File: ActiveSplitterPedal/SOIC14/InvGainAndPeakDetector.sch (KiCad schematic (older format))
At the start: 9 parts, among them U1 TL074

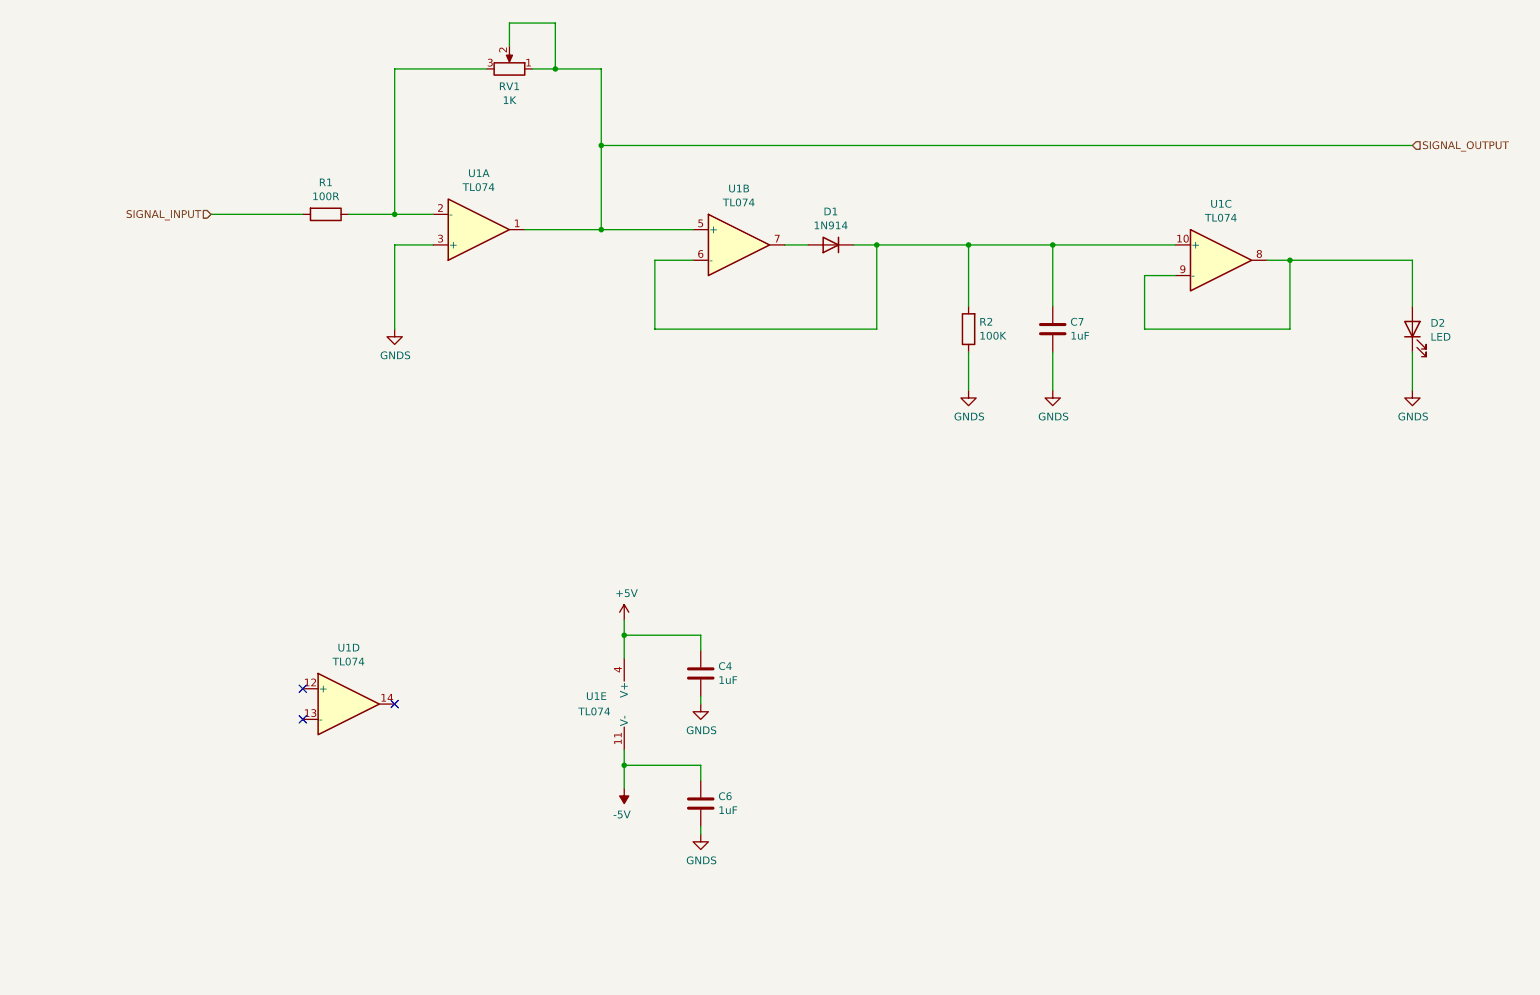
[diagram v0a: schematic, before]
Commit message: RevA HW updates
- Replaced SW Diode with Schottky Diode
- Added one charge pump IC per quad opamp (60mA each)
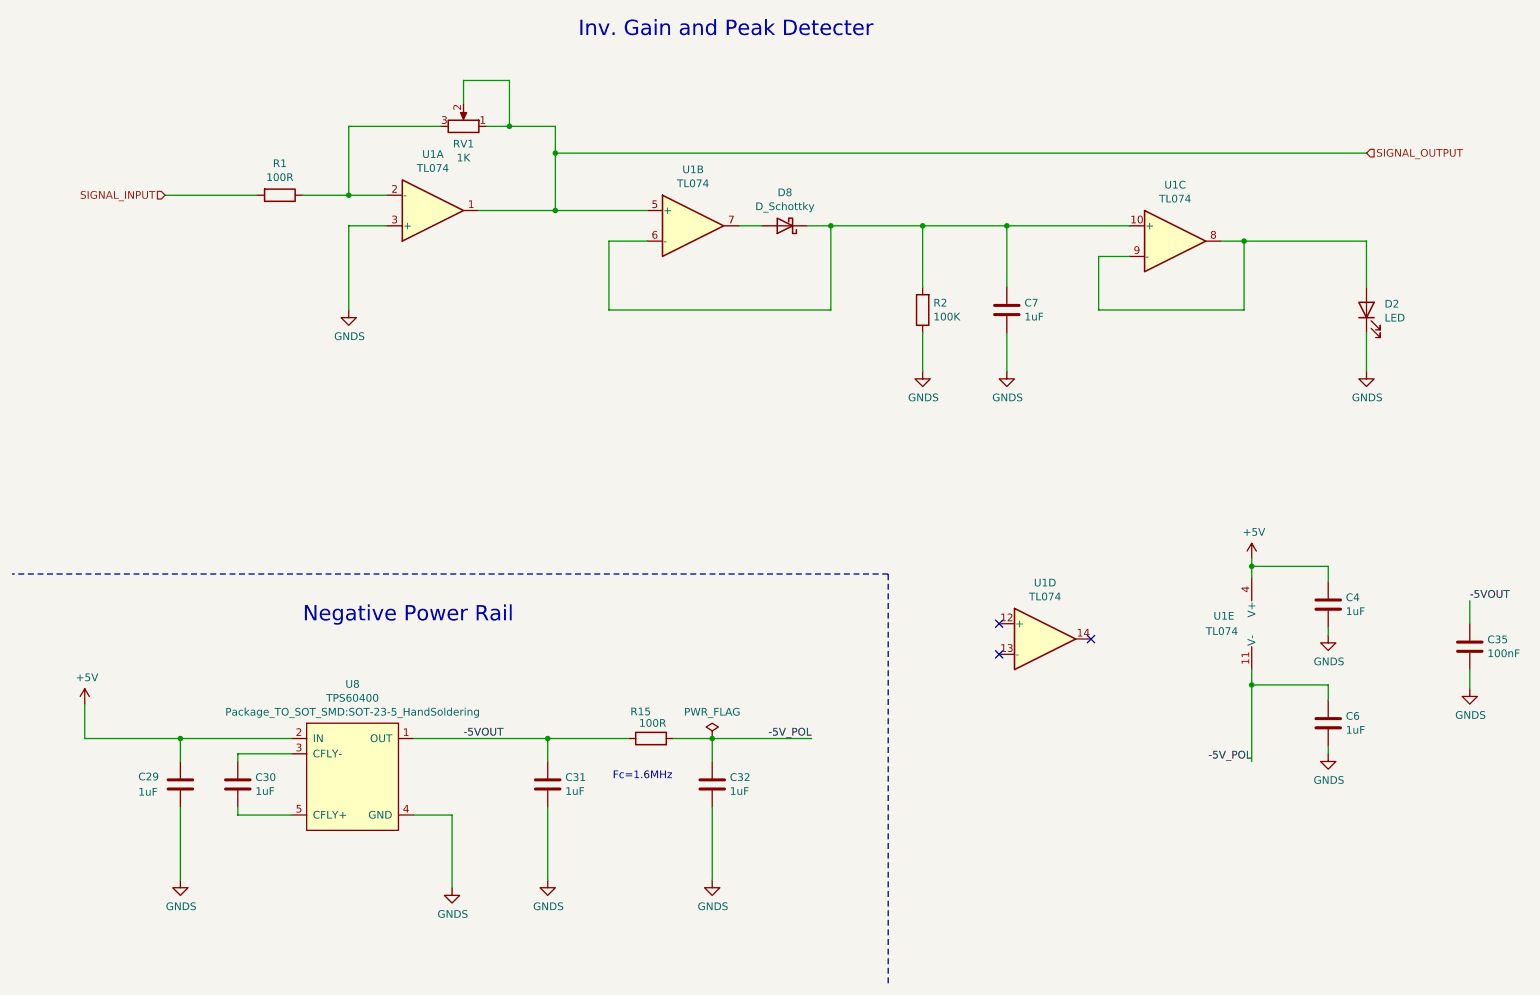
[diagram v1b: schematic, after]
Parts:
- removed D1: 1N914, Diode_SMD:D_SMB_Handsoldering, symbol Device:D
- added C1, C11, C2, C9: 1uF, Capacitor_SMD:C_0805_2012Metric_Pad1.15x1.40mm_HandSolder, symbol Device:C
- added C3: 100nF, Capacitor_SMD:C_0805_2012Metric_Pad1.15x1.40mm_HandSolder, symbol Device:C
- added D8: D_Schottky, Diode_SMD:D_SMB_Handsoldering, symbol Device:D_Schottky
- added R8: 100R, Resistor_SMD:R_0805_2012Metric_Pad1.15x1.40mm_HandSolder, symbol Device:R
- added U5: TPS60400, Package_TO_SOT_SMD:SOT-23-5_HandSoldering, symbol TPS6040x:TPS60400
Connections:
- net +5V: now also C1.1, U5.2 (IN)
- net GNDS: now also C1.2, C11.2, C3.2, C9.2, U5.4 (GND)
- net at C7.1, R2.2, U1.10 (+)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: now also D8.1 (K)
- net at U1.7: now also D8.2 (A)
- net -5V renamed -5V_POL
- net -5V_POL: now also C11.1, R8.2
- new net: C2.1, U5.3 (CFLY-)
- new net: C2.2, U5.5 (CFLY+)
- new net -5VOUT: C3.1, C9.1, R8.1, U5.1 (OUT)
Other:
- note added: "Fc=1.6MHz"
- note added: "Inv. Gain and Peak Detecter"
- note added: "Negative Power Rail"
- moved on the sheet: C4, C6, C7, D2, R1, R2, RV1, U1A, U1B, U1C, U1D, U1E
